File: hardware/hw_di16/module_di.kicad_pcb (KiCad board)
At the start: 2 copper layers, 141 parts, among them P1 DEBUG, P2 DI_0, P3 DI_1, U1 STM32F103C8Tx, U2 TLP291-4, U3 TLP291-4, U4 TLP291-4, U5 TLP291-4

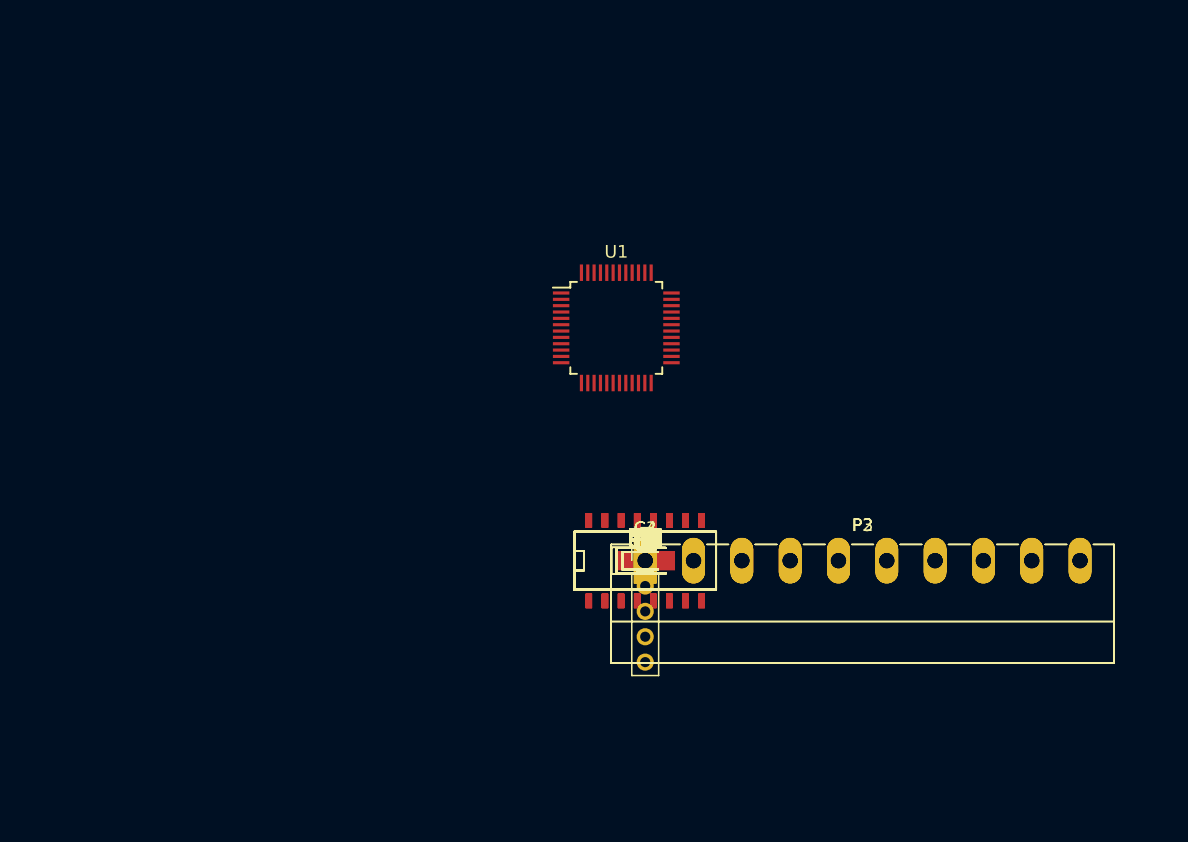
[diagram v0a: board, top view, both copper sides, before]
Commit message: Обновлена плата DI16.
Завершена предварительная разводка.
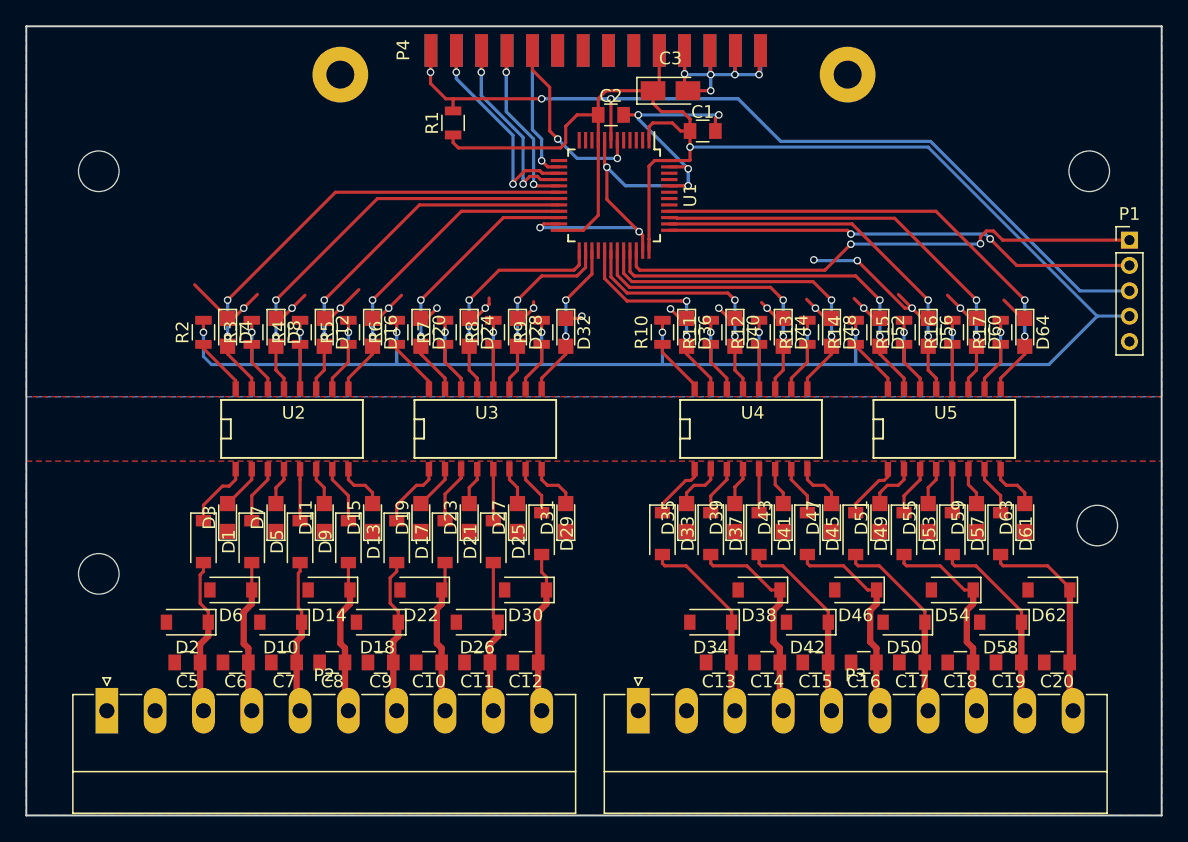
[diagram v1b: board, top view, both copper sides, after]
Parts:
- removed C4: 4,7u 10v, Capacitors_Tantalum_SMD:CP_Tantalum_Case-A_EIA-3216-18_Reflow
- removed D65, D66, D67, D68, D69, D70, D71, D72, D73, D74, D75, D76, D77, D78, D79, D80: LED, LEDs:LED_0805
- removed R18, R19, R20, R21, R22, R23, R24, R25, R26, R27, R28, R29, R30, R31, R32, R33: 300, Resistors_SMD:R_0805
- added P4: MOD_IN, Projects:Pin_Header_2.00mm_SMD, F.Cu at (144.6, 64.7)
- added REF**: MountingHole_3.2mm_M3, Mounting_Holes:MountingHole_3.2mm_M3, F.Cu at (105.4, 106.0)
- added REF**: MountingHole_3.2mm_M3, Mounting_Holes:MountingHole_3.2mm_M3, F.Cu at (105.4, 74.3)
- added REF**: MountingHole_3.2mm_M3, Mounting_Holes:MountingHole_3.2mm_M3, F.Cu at (184.2, 102.2)
- added REF**: MountingHole_3.2mm_M3, Mounting_Holes:MountingHole_3.2mm_M3, F.Cu at (183.5, 74.3)
- added REF**: MountingHole_2.2mm_M2_Pad, Mounting_Holes:MountingHole_2.2mm_M2_Pad, F.Cu at (124.5, 66.7)
- added REF**: MountingHole_2.2mm_M2_Pad, Mounting_Holes:MountingHole_2.2mm_M2_Pad, F.Cu at (164.5, 66.7)
- moved P1 45.8 mm to (186.7, 79.7)
- moved P2 44.1 mm to (106.0, 116.8)
- moved R2 39.2 mm to (113.7, 87.0), turned to 90 degrees
- moved R1 37.7 mm to (133.3, 70.5), turned to 90 degrees
- moved D4 37.5 mm to (115.6, 87.0), turned to 270 degrees
- moved C3 37.1 mm to (150.5, 67.9)
- moved C5 37.0 mm to (112.4, 113.0), turned to 180 degrees
- moved D2 36.4 mm to (112.4, 109.9), turned to 180 degrees
- moved R3 35.9 mm to (117.5, 87.0), turned to 90 degrees
- moved C2 35.3 mm to (145.8, 69.8)
- moved D64 34.9 mm to (178.4, 87.0), turned to 270 degrees
- moved D1 34.9 mm to (113.7, 103.5), turned to 270 degrees
- moved D8 34.2 mm to (119.4, 87.0), turned to 270 degrees
- moved C1 34.2 mm to (153.0, 71.1)
- moved C20 33.5 mm to (181.0, 113.0), turned to 180 degrees
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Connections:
- U1 pad 10: DI4 -> Net-(U1-Pad10)
- U1 pad 11: DI5 -> Net-(U1-Pad11)
- U1 pad 12: DI6 -> Net-(U1-Pad12)
- U1 pad 13: DI7 -> Net-(U1-Pad13)
- U1 pad 18: Net-(U1-Pad18) -> DI0
- U1 pad 19: Net-(U1-Pad19) -> DI1
- U1 pad 2: DI1 -> Net-(U1-Pad2)
- U1 pad 20: Net-(U1-Pad20) -> DI2
- U1 pad 21: Net-(U1-Pad21) -> DI3
- U1 pad 22: Net-(U1-Pad22) -> DI4
- U1 pad 25: DI8 -> DI5
- U1 pad 26: DI9 -> DI6
- U1 pad 27: DI10 -> DI7
- U1 pad 28: DI11 -> Net-(U1-Pad28)
- U1 pad 29: DI12 -> DI8
- U1 pad 3: DI2 -> Net-(U1-Pad3)
- U1 pad 30: DI13 -> DI9
- U1 pad 31: DI14 -> DI10
- U1 pad 32: DI15 -> DI11
- U1 pad 33: Net-(U1-Pad33) -> DI12
- U1 pad 38: Net-(U1-Pad38) -> DI13
- U1 pad 39: Net-(U1-Pad39) -> DI14
- U1 pad 4: DI3 -> Net-(U1-Pad4)
- U1 pad 40: Net-(U1-Pad40) -> DI15
- U1 pad 46: DI0 -> Net-(U1-Pad46)
- U2 pad 1: Net-(D13-Pad1) -> Net-(D1-Pad1)
- U2 pad 10: Net-(R2-Pad1) -> Net-(R5-Pad1)
- U2 pad 11: DI1 -> DI2
- U2 pad 12: Net-(R3-Pad1) -> Net-(R4-Pad1)
- U2 pad 13: DI2 -> DI1
- U2 pad 14: Net-(R4-Pad1) -> Net-(R3-Pad1)
- U2 pad 15: DI3 -> DI0
- U2 pad 16: Net-(R5-Pad1) -> Net-(R2-Pad1)
- U2 pad 2: Net-(D15-Pad2) -> Net-(D3-Pad2)
- U2 pad 3: Net-(D9-Pad1) -> Net-(D5-Pad1)
- U2 pad 4: Net-(D11-Pad2) -> Net-(D7-Pad2)
- U2 pad 5: Net-(D5-Pad1) -> Net-(D9-Pad1)
- U2 pad 6: Net-(D7-Pad2) -> Net-(D11-Pad2)
- U2 pad 7: Net-(D1-Pad1) -> Net-(D13-Pad1)
- U2 pad 8: Net-(D3-Pad2) -> Net-(D15-Pad2)
- U2 pad 9: DI0 -> DI3
- U3 pad 1: Net-(D29-Pad1) -> Net-(D17-Pad1)
- U3 pad 10: Net-(R6-Pad1) -> Net-(R9-Pad1)
- U3 pad 11: DI5 -> DI6
- U3 pad 12: Net-(R7-Pad1) -> Net-(R8-Pad1)
- U3 pad 13: DI6 -> DI5
- U3 pad 14: Net-(R8-Pad1) -> Net-(R7-Pad1)
- U3 pad 15: DI7 -> DI4
- U3 pad 16: Net-(R9-Pad1) -> Net-(R6-Pad1)
- U3 pad 2: Net-(D31-Pad2) -> Net-(D19-Pad2)
- U3 pad 3: Net-(D25-Pad1) -> Net-(D21-Pad1)
- U3 pad 4: Net-(D27-Pad2) -> Net-(D23-Pad2)
- U3 pad 5: Net-(D21-Pad1) -> Net-(D25-Pad1)
- U3 pad 6: Net-(D23-Pad2) -> Net-(D27-Pad2)
- U3 pad 7: Net-(D17-Pad1) -> Net-(D29-Pad1)
- U3 pad 8: Net-(D19-Pad2) -> Net-(D31-Pad2)
- U3 pad 9: DI4 -> DI7
- U4 pad 1: Net-(D45-Pad1) -> Net-(D33-Pad1)
- U4 pad 10: Net-(R10-Pad1) -> Net-(R13-Pad1)
- U4 pad 11: DI9 -> DI10
- U4 pad 12: Net-(R11-Pad1) -> Net-(R12-Pad1)
- U4 pad 13: DI10 -> DI9
- U4 pad 14: Net-(R12-Pad1) -> Net-(R11-Pad1)
- U4 pad 15: DI11 -> DI8
- U4 pad 16: Net-(R13-Pad1) -> Net-(R10-Pad1)
- U4 pad 2: Net-(D47-Pad2) -> Net-(D35-Pad2)
- U4 pad 3: Net-(D41-Pad1) -> Net-(D37-Pad1)
- U4 pad 4: Net-(D43-Pad2) -> Net-(D39-Pad2)
- U4 pad 5: Net-(D37-Pad1) -> Net-(D41-Pad1)
- U4 pad 6: Net-(D39-Pad2) -> Net-(D43-Pad2)
- U4 pad 7: Net-(D33-Pad1) -> Net-(D45-Pad1)
- U4 pad 8: Net-(D35-Pad2) -> Net-(D47-Pad2)
- U4 pad 9: DI8 -> DI11
- U5 pad 1: Net-(D61-Pad1) -> Net-(D49-Pad1)
- U5 pad 10: Net-(R14-Pad1) -> Net-(R17-Pad1)
- U5 pad 11: DI13 -> DI14
- U5 pad 12: Net-(R15-Pad1) -> Net-(R16-Pad1)
- U5 pad 13: DI14 -> DI13
- U5 pad 14: Net-(R16-Pad1) -> Net-(R15-Pad1)
- U5 pad 15: DI15 -> DI12
- U5 pad 16: Net-(R17-Pad1) -> Net-(R14-Pad1)
- U5 pad 2: Net-(D63-Pad2) -> Net-(D51-Pad2)
- U5 pad 3: Net-(D57-Pad1) -> Net-(D53-Pad1)
- U5 pad 4: Net-(D59-Pad2) -> Net-(D55-Pad2)
- U5 pad 5: Net-(D53-Pad1) -> Net-(D57-Pad1)
- U5 pad 6: Net-(D55-Pad2) -> Net-(D59-Pad2)
- U5 pad 7: Net-(D49-Pad1) -> Net-(D61-Pad1)
- U5 pad 8: Net-(D51-Pad2) -> Net-(D63-Pad2)
- U5 pad 9: DI12 -> DI15
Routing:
- net VDD: track 0.00 -> 225.0 mm, vias 0 -> 17
- net VSS: track 0.00 -> 124.0 mm, vias 0 -> 29
- net RESET: track 0.00 -> 70.5 mm, vias 0 -> 3
- net SWDIO: track 0.00 -> 42.2 mm, vias 0 -> 2
- net DI15: track 0.00 -> 38.7 mm, vias 0 -> 2
- net SWCLK: track 0.00 -> 37.4 mm, vias 0 -> 2
- net DI0: track 0.00 -> 37.4 mm, vias 0 -> 2
- net DI14: track 0.00 -> 34.2 mm, vias 0 -> 2
- net DI1: track 0.00 -> 32.9 mm, vias 0 -> 2
- net DI13: track 0.00 -> 30.2 mm, vias 0 -> 2
- net DI12: track 0.00 -> 30.1 mm, vias 0 -> 2
- net DI2: track 0.00 -> 28.9 mm, vias 0 -> 2
- net DI11: track 0.00 -> 26.8 mm, vias 0 -> 2
- net DI3: track 0.00 -> 25.4 mm, vias 0 -> 2
- net DI10: track 0.00 -> 23.1 mm, vias 0 -> 2
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- added copper zone on F.Cu, net DI0v
- added copper zone on B.Cu, net VSS
- added copper zone on F.Cu, net VSS
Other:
- board outline added: 89.5 x 62.2 mm
- rule pad_to_mask_clearance: 0.2 -> 0.18

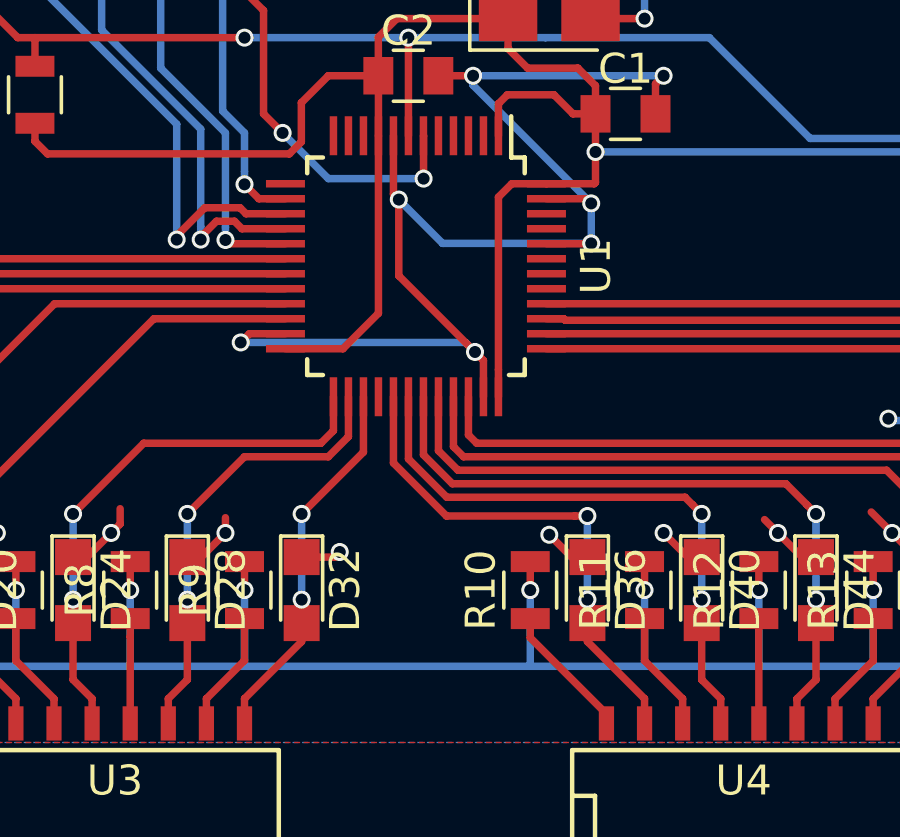
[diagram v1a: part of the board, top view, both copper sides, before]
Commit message: Обновлена плата модуля DI16.
Добавлены статусные светодиоды.
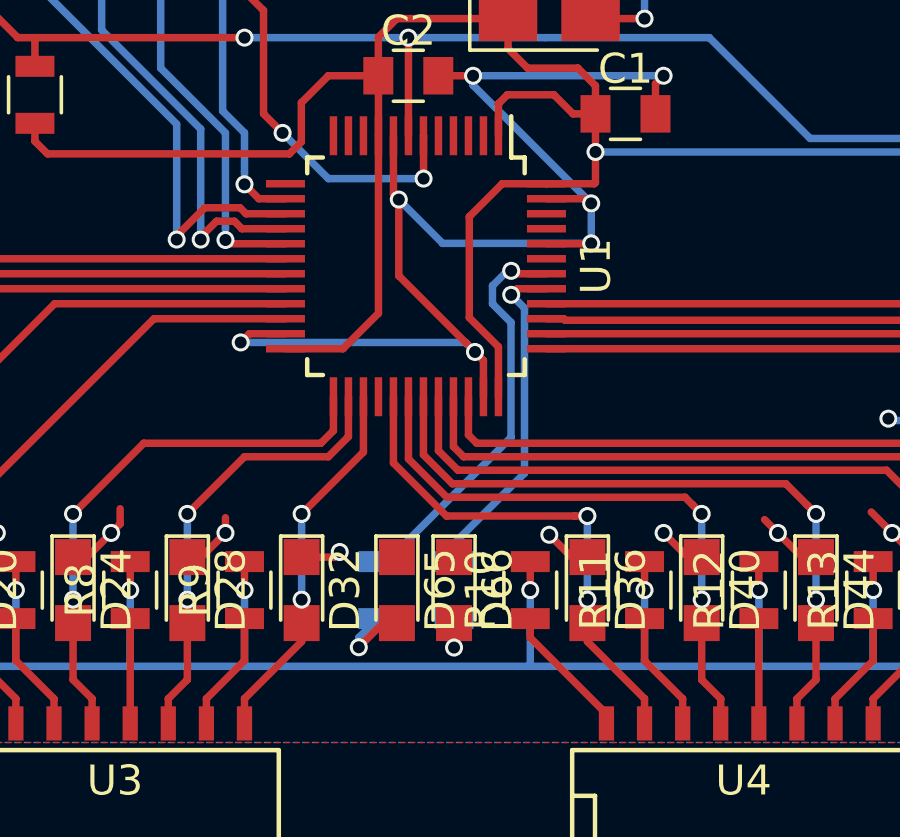
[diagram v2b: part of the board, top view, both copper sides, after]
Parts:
- added D65: SOK, LEDs:LED_0805, F.Cu at (145.4, 87.0)
- added D66: SFL, LEDs:LED_0805, F.Cu at (147.3, 87.0)
- added R18: 1k, Resistors_SMD:R_0805, B.Cu at (144.8, 87.0)
- added R19: 1k, Resistors_SMD:R_0805, B.Cu at (147.3, 87.0)
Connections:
- U1 pad 41: Net-(U1-Pad41) -> SFL
- U1 pad 42: Net-(U1-Pad42) -> SOK
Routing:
- net SOK: track 0.00 -> 13.5 mm, vias 0 -> 1
- net SFL: track 0.00 -> 11.3 mm, vias 0 -> 1
- net Net-(D65-Pad2): track 0.00 -> 2.82 mm, vias 0 -> 1
- net Net-(D66-Pad2): track 0.00 -> 1.78 mm, vias 0 -> 1
- net VDD: track 225.0 -> 225.9 mm

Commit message: Обновлена шелкография на платах.
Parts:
- D11, D12, D15, D16, D19, D20, D23, D24, D27, D28, D3, D31, D32, D35, D36, D39, D4, D40, D43, D44, D47, D48, D51, D52, D55, D56, D59, D60, D63, D64, D65, D66, D7, D8: footprint LEDs:LED_0805 -> LEDs:LED_0603
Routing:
- net VSS: track 124.0 -> 73.3 mm, vias 29 -> 12
- net (no net): track 0.00 -> 15.0 mm, vias 0 -> 2
- net DI3: track 25.4 -> 26.3 mm
- net DI15: track 38.7 -> 39.6 mm
- net DI11: track 26.8 -> 27.8 mm
- net DI0: track 37.4 -> 38.3 mm
- net DI9: track 19.9 -> 20.8 mm
- net DI8: track 17.1 -> 18.0 mm
- net DI7: track 12.5 -> 13.4 mm
- net DI6: track 15.0 -> 15.9 mm
- net DI5: track 18.2 -> 19.1 mm
- net DI4: track 21.4 -> 22.3 mm
- net DI2: track 28.9 -> 29.8 mm
- net DI14: track 34.2 -> 35.1 mm
- net DI13: track 30.2 -> 31.1 mm
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
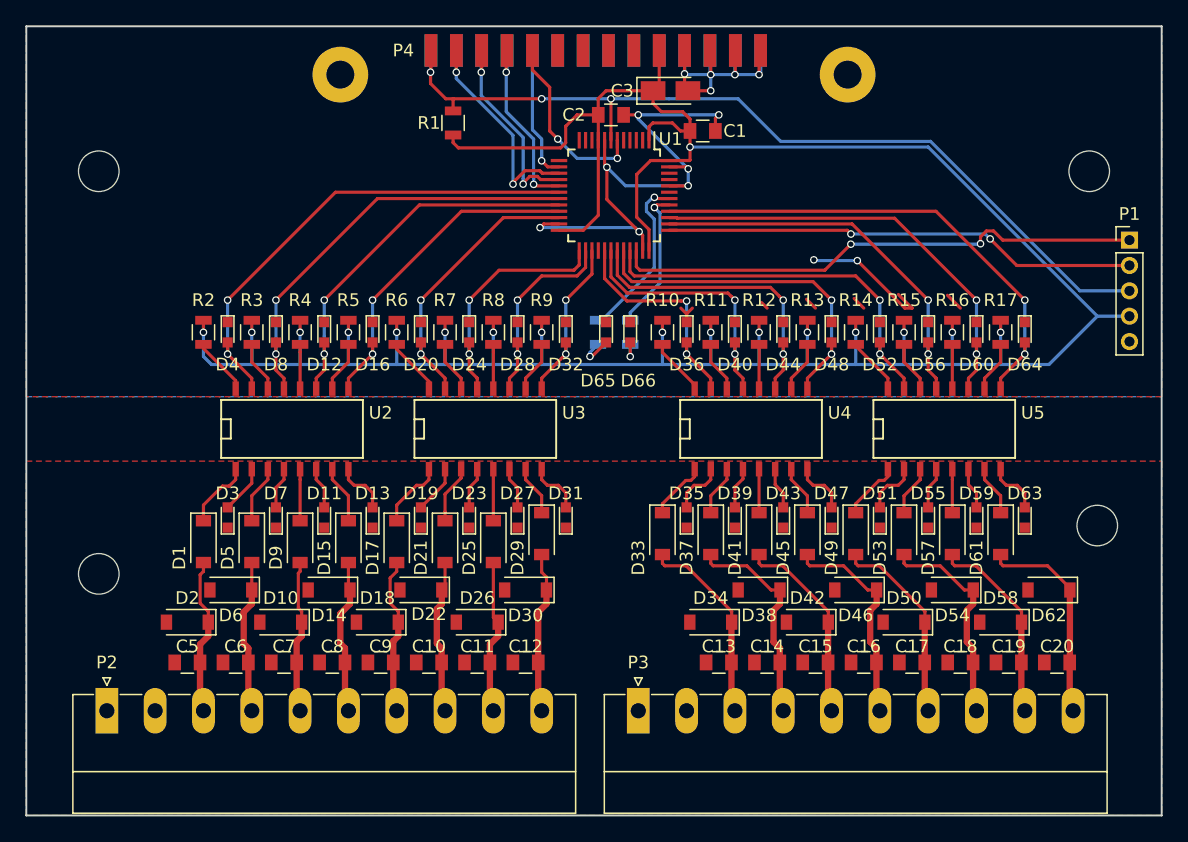
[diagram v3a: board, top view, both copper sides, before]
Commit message: Обновлены платы модулей - приведены к единому виду.
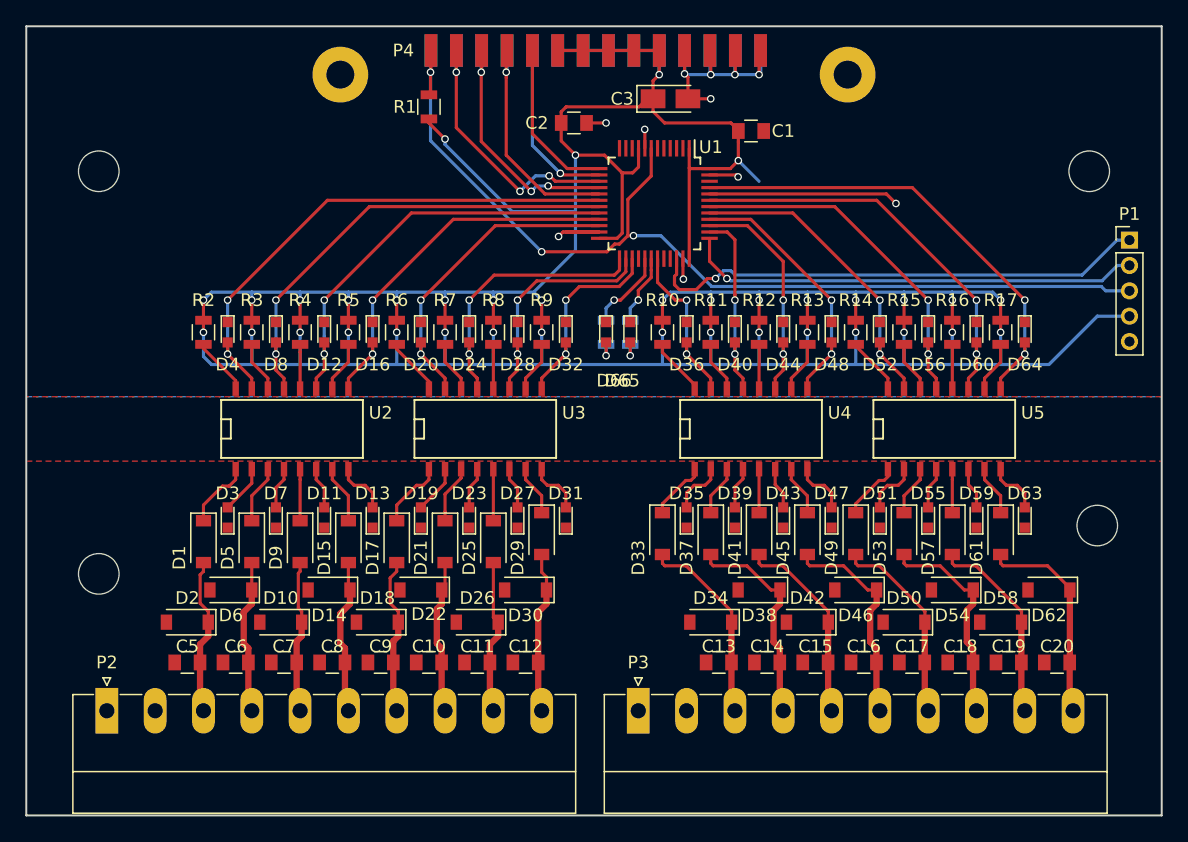
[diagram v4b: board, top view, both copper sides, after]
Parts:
- moved C1 3.81 mm to (156.8, 71.1)
- moved U1 3.24 mm to (149.2, 76.8)
- moved C2 2.99 mm to (142.9, 70.5)
- moved R18 2.54 mm to (147.3, 87.0)
- moved R1 2.29 mm to (131.4, 69.2)
- moved D65 1.91 mm to (147.3, 87.0)
- moved D66 1.91 mm to (145.4, 87.0)
- moved R19 1.91 mm to (145.4, 87.0)
- moved C3 0.64 mm to (150.5, 68.6)
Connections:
- U1 pad 13: Net-(U1-Pad13) -> SEL_OUT
- U1 pad 29: DI8 -> SFL
- U1 pad 30: DI9 -> SOK
- U1 pad 31: DI10 -> DI8
- U1 pad 32: DI11 -> Net-(U1-Pad32)
- U1 pad 33: DI12 -> Net-(U1-Pad33)
- U1 pad 38: DI13 -> DI9
- U1 pad 39: DI14 -> DI10
- U1 pad 40: DI15 -> DI11
- U1 pad 41: SFL -> DI12
- U1 pad 42: SOK -> DI13
- U1 pad 43: Net-(U1-Pad43) -> DI14
- U1 pad 45: Net-(U1-Pad45) -> DI15
- U1 pad 6: SEL_OUT -> Net-(U1-Pad6)
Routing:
- net VDD: track 225.9 -> 317.9 mm, vias 17 -> 36
- net VSS: track 73.3 -> 53.1 mm, vias 12 -> 11
- net (no net): track 15.0 -> 0.00 mm, vias 2 -> 0
- net RESET: track 70.5 -> 79.4 mm
- net SOK: track 13.5 -> 5.55 mm
- net DI11: track 27.8 -> 21.0 mm
- net DI12: track 31.0 -> 25.0 mm
- net DI10: track 24.0 -> 18.2 mm
- net DI9: track 20.8 -> 15.2 mm
- net SFL: track 11.3 -> 6.43 mm
- net DI8: track 18.0 -> 13.4 mm
- net SPI_SCK: track 18.3 -> 21.8 mm, vias 2 -> 3
- net SPI_MOSI: track 15.3 -> 18.6 mm, vias 2 -> 1
- net SPI_MISO: track 16.9 -> 20.1 mm, vias 2 -> 3
- net SEL_IN: track 10.8 -> 14.0 mm
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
